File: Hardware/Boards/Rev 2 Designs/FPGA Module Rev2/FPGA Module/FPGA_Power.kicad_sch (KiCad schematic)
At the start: 41 parts, among them U1 XCKU3P-FFVA676

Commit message: FPGA Module Rev 2 Layout Begun
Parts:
- removed C12, C13, C14, C15, C16, C17, C18, C19, C24, C25: 4.7uF, Capacitor_SMD:C_0201_0603Metric, symbol Device:C_Small
- renumbered C23 to C10, C26 to C11, C27 to C12, C28 to C13, C29 to C14, C30 to C15, C31 to C16, C32 to C17, C33 to C18, C34 to C19, C35 to C20, C36 to C21, C37 to C22, C38 to C23, C39 to C24, C40 to C25, C41 to C26, C42 to C27, C43 to C28, C8 to C3, C9 to C4, C10 to C5, C11 to C6, C20 to C7, C21 to C8, C22 to C9, R32 to R24, R33 to R25, R34 to R26, R35 to R27
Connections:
- net +0V9 is gone; now on net GND: U1.AA6 (MGTAVCC_R), U1.AC6 (MGTAVCC_R), U1.AE6 (MGTAVCC_R), U1.C6 (MGTAVCC_R), U1.E6 (MGTAVCC_R), U1.G6 (MGTAVCC_R), U1.L6 (MGTAVCC_R), U1.N6 (MGTAVCC_R), U1.R6 (MGTAVCC_R), U1.U6 (MGTAVCC_R)
- net +1V2: no longer U1.AC2 (MGTAVTT_R), U1.AD3 (MGTAVTT_R), U1.C2 (MGTAVTT_R), U1.D3 (MGTAVTT_R), U1.G2 (MGTAVTT_R), U1.H3 (MGTAVTT_R), U1.L2 (MGTAVTT_R), U1.M3 (MGTAVTT_R), U1.R2 (MGTAVTT_R), U1.T3 (MGTAVTT_R), U1.W2 (MGTAVTT_R), U1.Y3 (MGTAVTT_R)
- net +1V8: no longer U1.J6 (MGTVCCAUX_R), U1.W6 (MGTVCCAUX_R)
- net GND: now also U1.AC2 (MGTAVTT_R), U1.AD3 (MGTAVTT_R), U1.C2 (MGTAVTT_R), U1.D3 (MGTAVTT_R), U1.G2 (MGTAVTT_R), U1.H3 (MGTAVTT_R), U1.J6 (MGTVCCAUX_R), U1.L2 (MGTAVTT_R), U1.M3 (MGTAVTT_R), U1.R2 (MGTAVTT_R), U1.T3 (MGTAVTT_R), U1.W2 (MGTAVTT_R), U1.W6 (MGTVCCAUX_R), U1.Y3 (MGTAVTT_R)

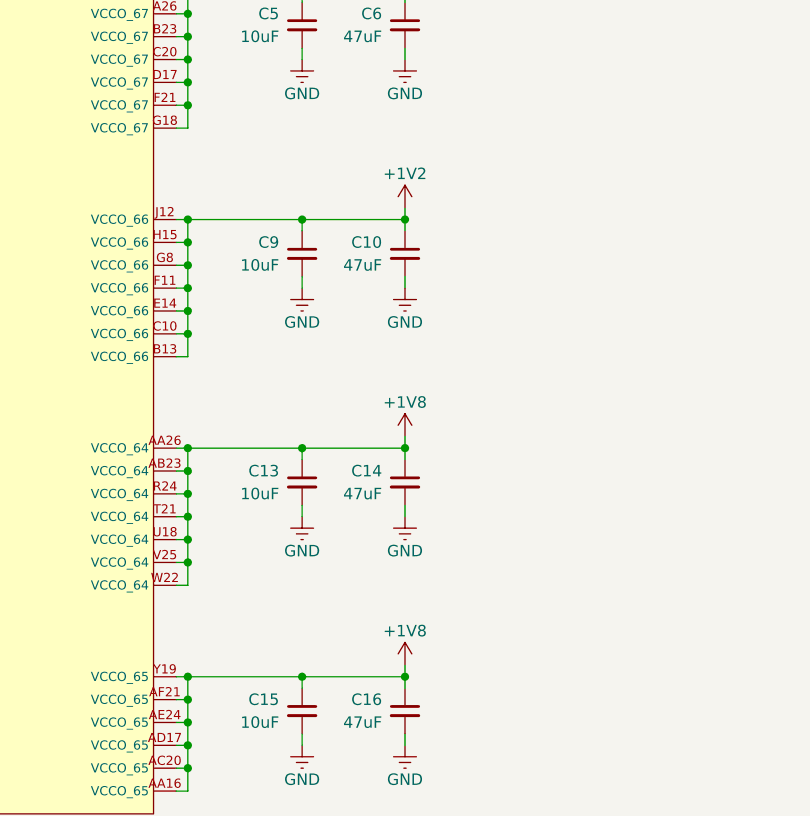
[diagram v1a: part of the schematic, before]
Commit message: Completed B2B and HyperRam routing
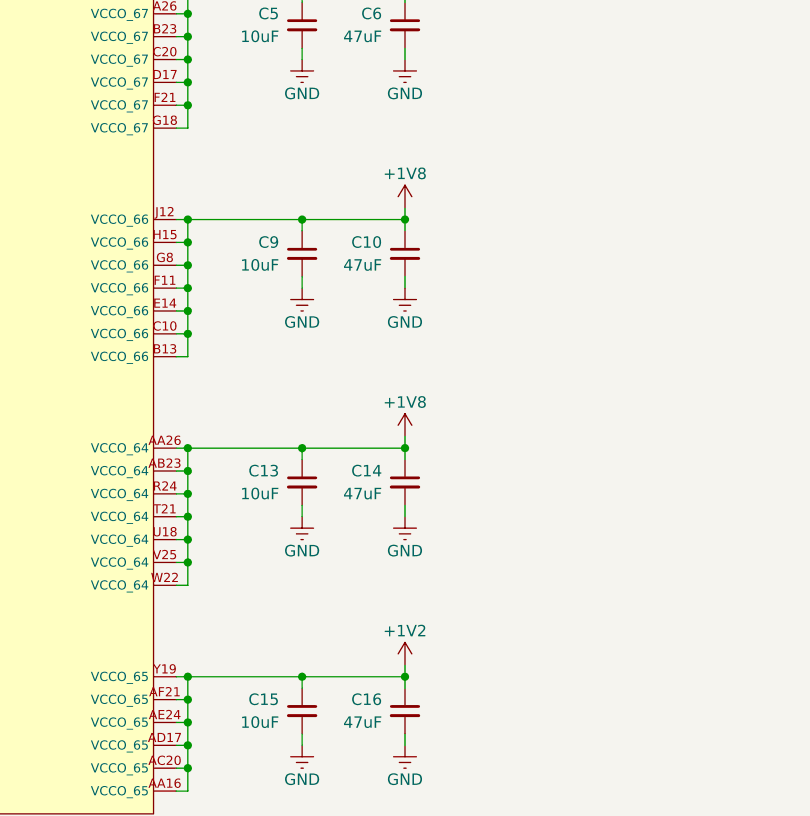
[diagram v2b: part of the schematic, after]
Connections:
- net +1V2: now also C15.1, C16.1, U1.AA16 (VCCO_65), U1.AC20 (VCCO_65), U1.AD17 (VCCO_65), U1.AE24 (VCCO_65), U1.AF21 (VCCO_65), U1.Y19 (VCCO_65); no longer C10.1, C9.1, U1.B13 (VCCO_66), U1.C10 (VCCO_66), U1.E14 (VCCO_66), U1.F11 (VCCO_66), U1.G8 (VCCO_66), U1.H15 (VCCO_66), U1.J12 (VCCO_66)
- net +1V8: now also C10.1, C9.1, U1.B13 (VCCO_66), U1.C10 (VCCO_66), U1.E14 (VCCO_66), U1.F11 (VCCO_66), U1.G8 (VCCO_66), U1.H15 (VCCO_66), U1.J12 (VCCO_66); no longer C15.1, C16.1, U1.AA16 (VCCO_65), U1.AC20 (VCCO_65), U1.AD17 (VCCO_65), U1.AE24 (VCCO_65), U1.AF21 (VCCO_65), U1.Y19 (VCCO_65)
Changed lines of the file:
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@@
 	)
 	(symbol
-		(lib_id "power:+1V2")
-		(at 280.67 69.85 0)
-		(unit 1)
-		(exclude_from_sim no)
-		(in_bom yes)
-		(on_board yes)
-		(dnp no)
-		(property "Reference" "#PWR040"
-			(at 280.67 73.66 0)
-			(effects
-				(font
-					(size 1.27 1.27)
-				)
-				(hide yes)
-			)
-		)
-		(property "Value" "+1V2"
-			(at 280.67 66.04 0)
-			(effects
-				(font
-					(size 1.27 1.27)
-				)
-			)
-		)
-		(property "Footprint" ""
-			(at 280.67 69.85 0)
-			(effects
-				(font
-					(size 1.27 1.27)
-				)
-				(hide yes)
-			)
-		)
-		(property "Datasheet" ""
-			(at 280.67 69.85 0)
-			(effects
-				(font
-					(size 1.27 1.27)
-				)
-				(hide yes)
-			)
-		)
-		(property "Description" "Power symbol creates a global label with name \"+1V2\""
-			(at 280.67 69.85 0)
-			(effects
-				(font
-					(size 1.27 1.27)
-				)
-				(hide yes)
-			)
-		)
-		(pin "1"
-		)
-		(instances
-			(project "FPGA Module"
-				(path "/199f10e2-d4b4-4a27-9e84-7b1ce2ae6bf0/0c296310-f788-47f0-8a3f-43c3444563e8/ff43e174-bde2-43ac-b61b-dc2c71092798"
-					(reference "#PWR040")
-					(unit 1)
-				)
-			)
-		)
-	)
-	(symbol
 		(lib_id "Device:C_Small")
 		(at 212.09 167.64 0)
@@
 	)
 	(symbol
-		(lib_id "power:GND")
-		(at 354.33 234.95 0)
+		(lib_id "power:+1V8")
+		(at 280.67 69.85 0)
+		(mirror y)
 		(unit 1)
 		(exclude_from_sim no)
@@
 		(on_board yes)
 		(dnp no)
-		(property "Reference" "#PWR069"
-			(at 354.33 241.3 0)
+		(property "Reference" "#PWR051"
+			(at 280.67 73.66 0)
 			(effects
 				(font
@@
 			)
 		)
-		(property "Value" "GND"
-			(at 354.33 238.76 0)
+		(property "Value" "+1V8"
+			(at 280.67 66.04 0)
 			(effects
 				(font
@@
 		)
 		(property "Footprint" ""
-			(at 354.33 234.95 0)
+			(at 280.67 69.85 0)
 			(effects
 				(font
@@
 		)
 		(property "Datasheet" ""
-			(at 354.33 234.95 0)
+			(at 280.67 69.85 0)
 			(effects
 				(font
@@
 			)
 		)
-		(property "Description" "Power symbol creates a global label with name \"GND\" , ground"
-			(at 354.33 234.95 0)
+		(property "Description" "Power symbol creates a global label with name \"+1V8\""
+			(at 280.67 69.85 0)
 			(effects
 				(font
@@
 			(project "FPGA Module"
 				(path "/199f10e2-d4b4-4a27-9e84-7b1ce2ae6bf0/0c296310-f788-47f0-8a3f-43c3444563e8/ff43e174-bde2-43ac-b61b-dc2c71092798"
-					(reference "#PWR069")
+					(reference "#PWR051")
 					(unit 1)
 				)
@@
 	)
 	(symbol
-		(lib_id "Device:R_US")
-		(at 217.17 109.22 270)
+		(lib_id "power:+1V2")
+		(at 280.67 120.65 0)
 		(unit 1)
 		(exclude_from_sim no)
@@
 		(on_board yes)
 		(dnp no)
-		(property "Reference" "R25"
-			(at 217.17 104.14 90)
+		(property "Reference" "#PWR040"
+			(at 280.67 124.46 0)
 			(effects
 				(font
 					(size 1.27 1.27)
 				)
+				(hide yes)
 			)
 		)
-		(property "Value" "1K"
-			(at 217.17 106.68 90)
+		(property "Value" "+1V2"
+			(at 280.67 116.84 0)
 			(effects
 				(font
@@
 			)
 		)
-		(property "Footprint" "Resistor_SMD:R_0201_0603Metric"
-			(at 216.916 110.236 90)
+		(property "Footprint" ""
+			(at 280.67 120.65 0)
 			(effects
 				(font
@@
 			)
 		)
-		(property "Datasheet" "~"
-			(at 217.17 109.22 0)
+		(property "Datasheet" ""
+			(at 280.67 120.65 0)
 			(effects
 				(font
@@
 			)
 		)
-		(property "Description" "Resistor, US symbol"
-			(at 217.17 109.22 0)
+		(property "Description" "Power symbol creates a global label with name \"+1V2\""
+			(at 280.67 120.65 0)
 			(effects
 				(font
@@
 		(pin "1"
 		)
-		(pin "2"
-		)
 		(instances
 			(project "FPGA Module"
 				(path "/199f10e2-d4b4-4a27-9e84-7b1ce2ae6bf0/0c296310-f788-47f0-8a3f-43c3444563e8/ff43e174-bde2-43ac-b61b-dc2c71092798"
-					(reference "R25")
+					(reference "#PWR040")
 					(unit 1)
 				)
@@
 	)
 	(symbol
-		(lib_id "power:+1V8")
-		(at 280.67 120.65 0)
-		(mirror y)
+		(lib_id "power:GND")
+		(at 354.33 234.95 0)
 		(unit 1)
 		(exclude_from_sim no)
@@
 		(on_board yes)
 		(dnp no)
-		(property "Reference" "#PWR051"
-			(at 280.67 124.46 0)
+		(property "Reference" "#PWR069"
+			(at 354.33 241.3 0)
 			(effects
 				(font
@@
 			)
 		)
-		(property "Value" "+1V8"
-			(at 280.67 116.84 0)
+		(property "Value" "GND"
+			(at 354.33 238.76 0)
 			(effects
 				(font
@@
 		)
 		(property "Footprint" ""
-			(at 280.67 120.65 0)
+			(at 354.33 234.95 0)
 			(effects
 				(font
@@
 		)
 		(property "Datasheet" ""
-			(at 280.67 120.65 0)
+			(at 354.33 234.95 0)
 			(effects
 				(font
@@
 			)
 		)
-		(property "Description" "Power symbol creates a global label with name \"+1V8\""
-			(at 280.67 120.65 0)
+		(property "Description" "Power symbol creates a global label with name \"GND\" , ground"
+			(at 354.33 234.95 0)
 			(effects
 				(font
@@
 			(project "FPGA Module"
 				(path "/199f10e2-d4b4-4a27-9e84-7b1ce2ae6bf0/0c296310-f788-47f0-8a3f-43c3444563e8/ff43e174-bde2-43ac-b61b-dc2c71092798"
-					(reference "#PWR051")
+					(reference "#PWR069")
+					(unit 1)
+				)
+			)
+		)
+	)
+	(symbol
+		(lib_id "Device:R_US")
+		(at 217.17 109.22 270)
+		(unit 1)
+		(exclude_from_sim no)
+		(in_bom yes)
+		(on_board yes)
+		(dnp no)
+		(property "Reference" "R25"
+			(at 217.17 104.14 90)
+			(effects
+				(font
+					(size 1.27 1.27)
+				)
+			)
+		)
+		(property "Value" "1K"
+			(at 217.17 106.68 90)
+			(effects
+				(font
+					(size 1.27 1.27)
+				)
+			)
+		)
+		(property "Footprint" "Resistor_SMD:R_0201_0603Metric"
+			(at 216.916 110.236 90)
+			(effects
+				(font
+					(size 1.27 1.27)
+				)
+				(hide yes)
+			)
+		)
+		(property "Datasheet" "~"
+			(at 217.17 109.22 0)
+			(effects
+				(font
+					(size 1.27 1.27)
+				)
+				(hide yes)
+			)
+		)
+		(property "Description" "Resistor, US symbol"
+			(at 217.17 109.22 0)
+			(effects
+				(font
+					(size 1.27 1.27)
+				)
+				(hide yes)
+			)
+		)
+		(pin "1"
+		)
+		(pin "2"
+		)
+		(instances
+			(project "FPGA Module"
+				(path "/199f10e2-d4b4-4a27-9e84-7b1ce2ae6bf0/0c296310-f788-47f0-8a3f-43c3444563e8/ff43e174-bde2-43ac-b61b-dc2c71092798"
+					(reference "R25")
 					(unit 1)
 				)
